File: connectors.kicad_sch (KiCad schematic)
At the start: 4 parts, among them J1 Conn_01x04_Pin, J2 Conn_01x04_Pin, J3 Conn_01x09_Pin, J4 Conn_02x03_Odd_Even

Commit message: Added footprints to components in schematic and added external library for external footprints
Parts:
- J1, J2: footprint (none) -> Connector_PinHeader_2.54mm:PinHeader_1x04_P2.54mm_Vertical
- J3: footprint (none) -> Connector_PinHeader_2.54mm:PinHeader_1x09_P2.54mm_Vertical
- J4: footprint (none) -> Connector_PinHeader_2.54mm:PinHeader_2x03_P2.54mm_Vertical
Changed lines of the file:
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@@
 			)
 		)
-		(property "Footprint" ""
+		(property "Footprint" "Connector_PinHeader_2.54mm:PinHeader_1x04_P2.54mm_Vertical"
 			(at 54.61 55.88 0)
 			(effects
@@
 			)
 		)
-		(property "Footprint" ""
+		(property "Footprint" "Connector_PinHeader_2.54mm:PinHeader_1x04_P2.54mm_Vertical"
 			(at 54.61 36.83 0)
 			(effects
@@
 			)
 		)
-		(property "Footprint" ""
+		(property "Footprint" "Connector_PinHeader_2.54mm:PinHeader_1x09_P2.54mm_Vertical"
 			(at 54.61 85.09 0)
 			(effects
@@
 			)
 		)
-		(property "Footprint" ""
+		(property "Footprint" "Connector_PinHeader_2.54mm:PinHeader_2x03_P2.54mm_Vertical"
 			(at 90.17 88.9 0)
 			(effects

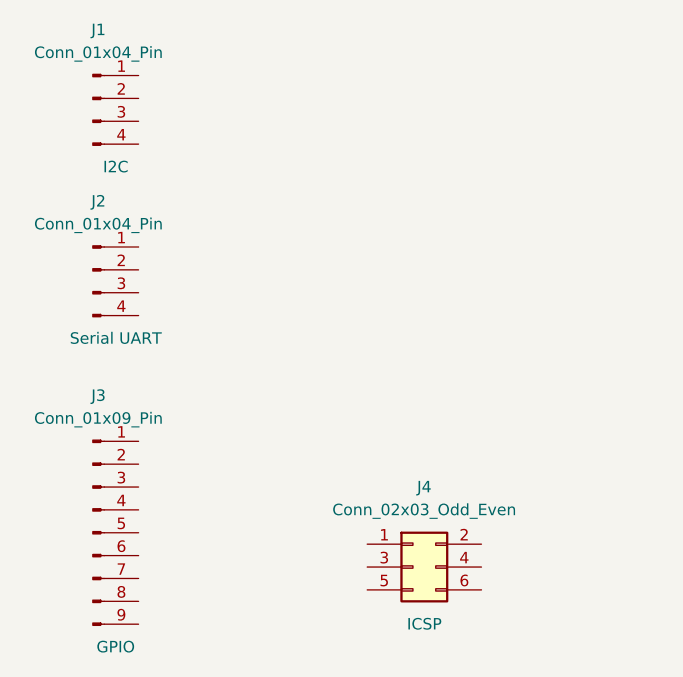
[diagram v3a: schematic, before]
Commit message: Completed schematic wiring and passed ERC
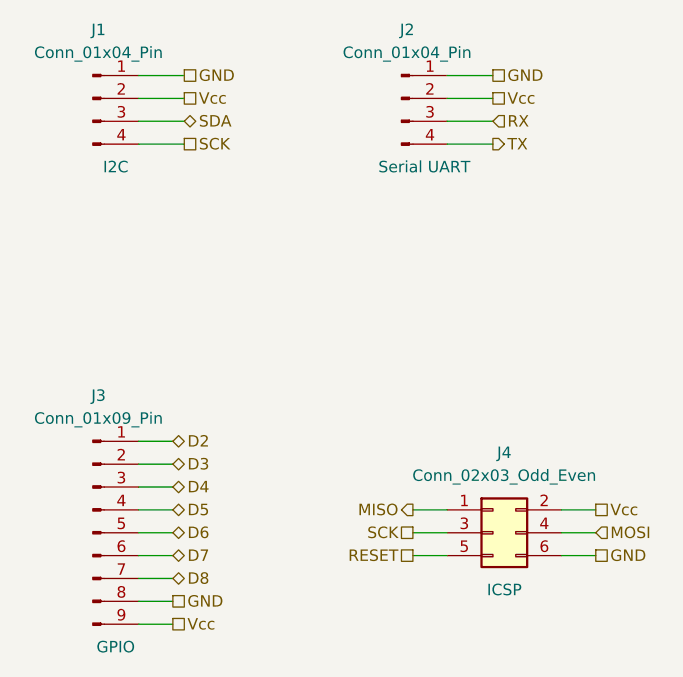
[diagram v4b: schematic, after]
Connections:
- net GND: now reaches J2.1 (Pin_1)
- net GND: now also J1.1 (Pin_1), J3.8 (Pin_8), J4.6 (Pin_6)
- net Vcc: now reaches J2.2 (Pin_2)
- net Vcc: now also J1.2 (Pin_2), J3.9 (Pin_9), J4.2 (Pin_2)
- net RX: now reaches J2.3 (Pin_3)
- net TX: now reaches J2.4 (Pin_4)
- net SDA: now reaches J1.3 (Pin_3)
- net SCK: now reaches J1.4 (Pin_4)
- net SCK: now also J4.3 (Pin_3)
- net D2: now reaches J3.1 (Pin_1)
- net D3: now reaches J3.2 (Pin_2)
- net D4: now reaches J3.3 (Pin_3)
- net D5: now reaches J3.4 (Pin_4)
- net D6: now reaches J3.5 (Pin_5)
- net D7: now reaches J3.6 (Pin_6)
- net D8: now reaches J3.7 (Pin_7)
- net MISO: now reaches J4.1 (Pin_1)
- net MOSI: now reaches J4.4 (Pin_4)
- net RESET: now reaches J4.5 (Pin_5)
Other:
- moved on the sheet: J2, J4

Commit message: fixed bug that affects the clock
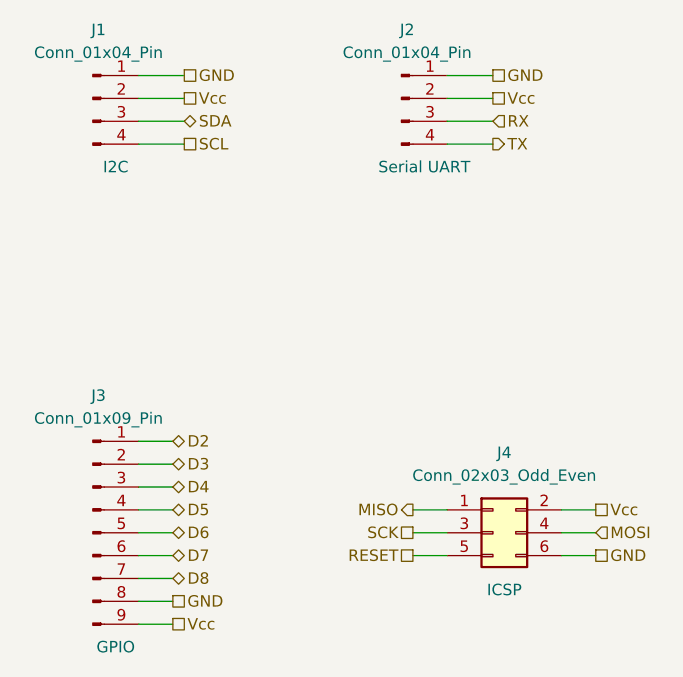
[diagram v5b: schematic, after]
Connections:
- net SCK: no longer J1.4 (Pin_4)
- new net SCL: J1.4 (Pin_4)
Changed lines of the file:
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@@
 		)
 	)
-	(hierarchical_label "SCK"
+	(hierarchical_label "SCL"
 		(shape passive)
 		(at 64.77 41.91 0)
